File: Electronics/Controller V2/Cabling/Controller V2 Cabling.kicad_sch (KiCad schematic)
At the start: 13 parts, among them J1 776164-1, J10 Spare Valve, J11 Battery, J12 776286-1, J2 GPIO, J3 Tractor CAN, J4 Scraper CAN, J5 Spare CAN, J6 Front Height, J7 Rear Height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

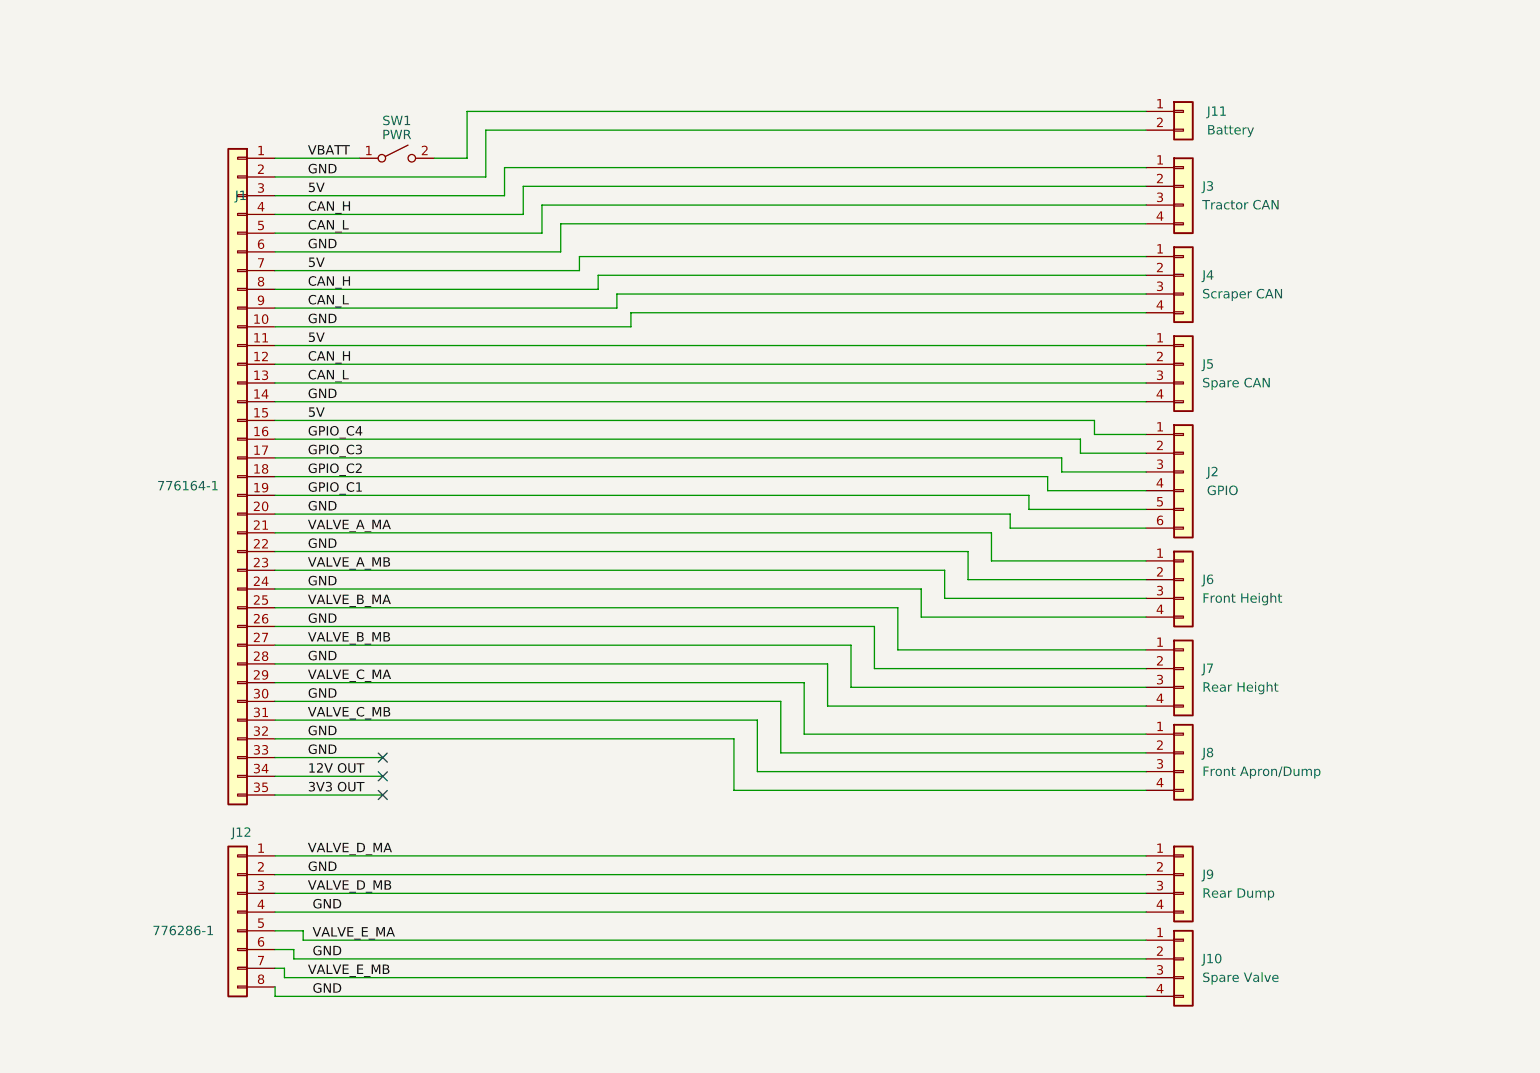
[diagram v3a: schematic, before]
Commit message: Working on autosteer support for V2 controller.
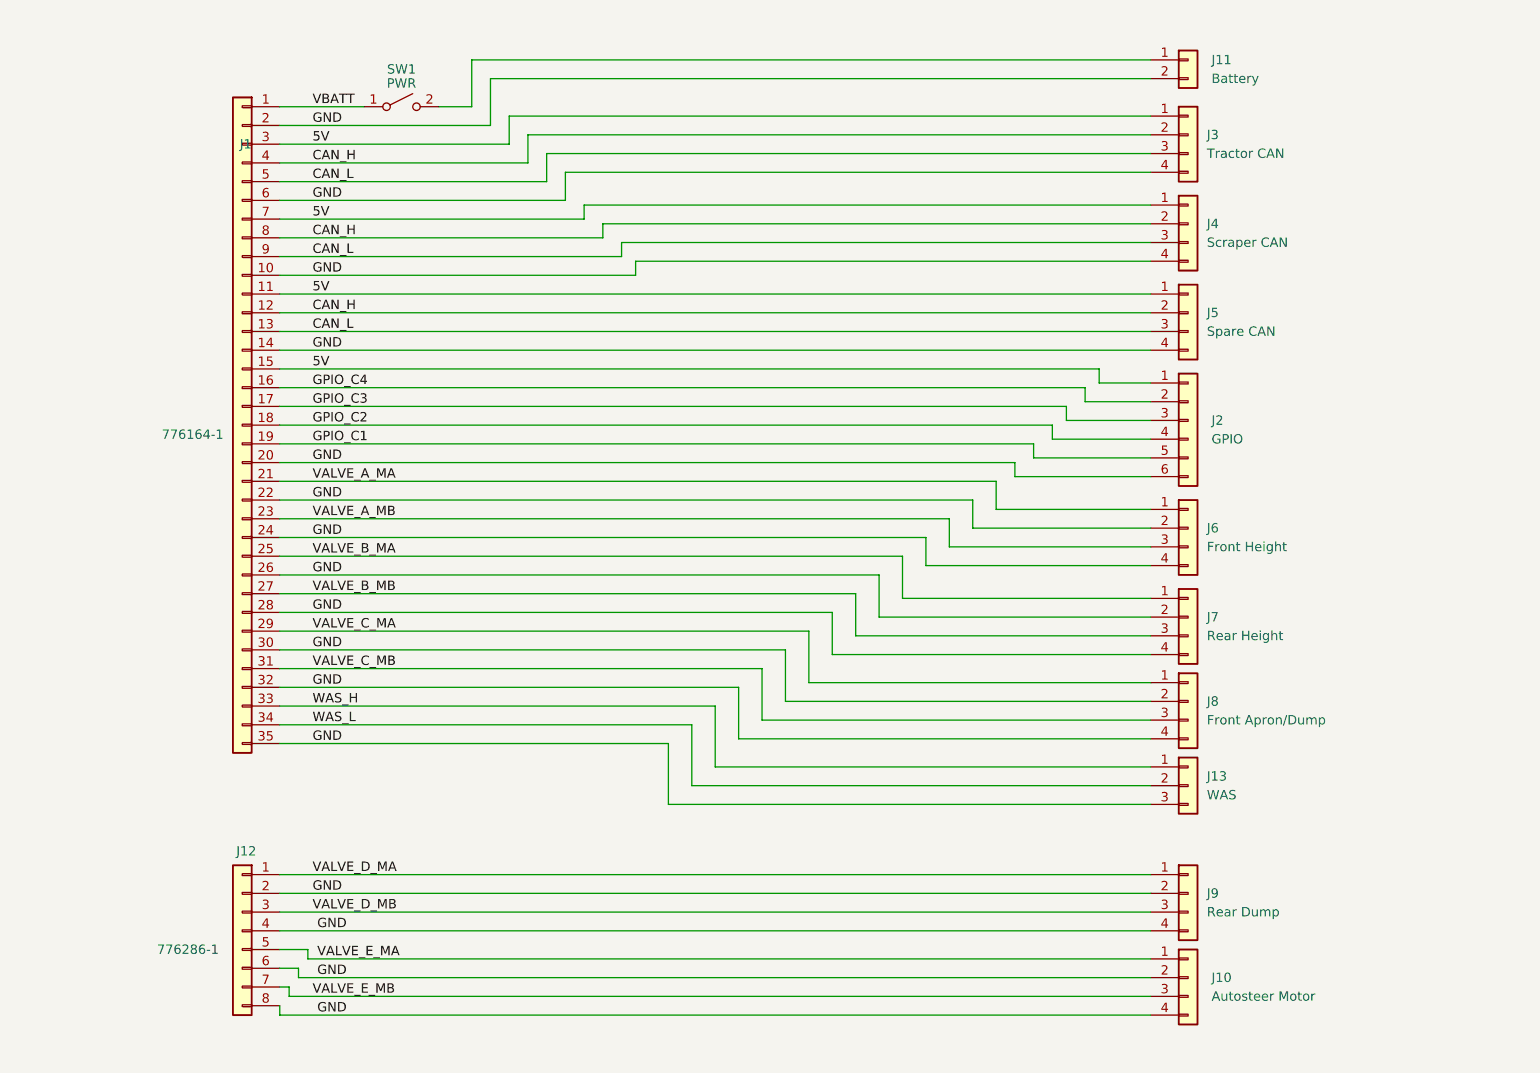
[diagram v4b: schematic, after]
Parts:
- added J13: WAS, symbol Connector_Generic:Conn_01x03
- J10: value Spare Valve -> Autosteer Motor
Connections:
- net 3V3 OUT is gone; now on net GND: J1.35 (Pin_35)
- net GND: now also J13.3 (Pin_3); no longer J1.33 (Pin_33)
- net 12V OUT renamed WAS_L
- net WAS_L: now also J13.2 (Pin_2)
- new net WAS_H: J1.33 (Pin_33), J13.1 (Pin_1)
- no-connect marks 3 -> 0
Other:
- moved on the sheet: J1, J10, J11, J12, J2, J3, J4, J5, J6, J7, J8, J9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

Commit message: Added WAS circuit.
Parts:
- J13: symbol Connector_Generic:Conn_01x03 -> Connector_Generic:Conn_01x04
- J2: symbol Connector_Generic:Conn_01x06 -> Connector_Generic:Conn_01x05
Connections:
- net 5V: now also J1.16 (Pin_16), J13.4 (Pin_4)
- net GND: now also J2.5 (Pin_5); no longer J2.6 (Pin_6)
- net GPIO_C1: now also J2.4 (Pin_4); no longer J2.5 (Pin_5)
- net GPIO_C2: now also J2.3 (Pin_3); no longer J2.4 (Pin_4)
- net GPIO_C3: now also J2.2 (Pin_2); no longer J2.3 (Pin_3)
- removed net GPIO_C4: J1.16 (Pin_16), J2.2 (Pin_2)
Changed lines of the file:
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@@
+    (stroke (width 0) (type default))
+  )
+  (wire (pts (xy 202.565 130.81) (xy 103.505 130.81))
     (stroke (width 0) (type default))
   )
@@
     (stroke (width 0) (type default))
   )
+  (wire (pts (xy 103.505 130.81) (xy 103.505 69.215))
+    (stroke (width 0) (type default))
+  )
   (wire (pts (xy 202.565 34.925) (xy 115.57 34.925))
     (stroke (width 0) (type default))
@@
     (stroke (width 0) (type default))
   )
-  (wire (pts (xy 202.565 71.12) (xy 195.58 71.12))
-    (stroke (width 0) (type default))
-  )
   (wire (pts (xy 84.455 74.295) (xy 191.135 74.295))
     (stroke (width 0) (type default))
@@
     (stroke (width 0) (type default))
   )
-  (wire (pts (xy 84.455 69.215) (xy 195.58 69.215))
-    (stroke (width 0) (type default))
-  )
   (wire (pts (xy 84.455 46.355) (xy 123.19 46.355))
     (stroke (width 0) (type default))
@@
     (stroke (width 0) (type default))
   )
+  (wire (pts (xy 84.455 69.215) (xy 103.505 69.215))
+    (stroke (width 0) (type default))
+  )
   (wire (pts (xy 202.565 52.07) (xy 130.81 52.07))
     (stroke (width 0) (type default))
@@
     (stroke (width 0) (type default))
   )
-  (wire (pts (xy 195.58 71.12) (xy 195.58 69.215))
-    (stroke (width 0) (type default))
-  )
   (wire (pts (xy 202.565 95.885) (xy 172.085 95.885))
     (stroke (width 0) (type default))
@@
     (effects (font (size 1.27 1.27)) (justify left bottom))
   )
-  (label "GPIO_C4" (at 88.9 71.755 0) (fields_autoplaced)
+  (label "5V" (at 88.9 71.755 0) (fields_autoplaced)
     (effects (font (size 1.27 1.27)) (justify left bottom))
   )
@@
     )
   )
-  (symbol (lib_id "Connector_Generic:Conn_01x06") (at 207.645 76.2 0) (unit 1)
-    (in_bom yes) (on_board yes) (dnp no) (fields_autoplaced)
-    (property "Reference" "J2" (at 210.82 76.2 0)
-      (effects (font (size 1.27 1.27)) (justify left))
-    )
-    (property "Value" "GPIO" (at 210.82 78.74 0)
-      (effects (font (size 1.27 1.27)) (justify left))
-    )
-    (property "Footprint" "" (at 207.645 76.2 0)
-      (effects (font (size 1.27 1.27)) hide)
-    )
-    (property "Datasheet" "~" (at 207.645 76.2 0)
+  (symbol (lib_id "Connector_Generic:Conn_01x05") (at 207.645 78.74 0) (unit 1)
+    (in_bom yes) (on_board yes) (dnp no) (fields_autoplaced)
+    (property "Reference" "J2" (at 210.82 77.47 0)
+      (effects (font (size 1.27 1.27)) (justify left))
+    )
+    (property "Value" "GPIO" (at 210.82 80.01 0)
+      (effects (font (size 1.27 1.27)) (justify left))
+    )
+    (property "Footprint" "" (at 207.645 78.74 0)
+      (effects (font (size 1.27 1.27)) hide)
+    )
+    (property "Datasheet" "~" (at 207.645 78.74 0)
       (effects (font (size 1.27 1.27)) hide)
     )
     (pin "5")
     (pin "1")
-    (pin "6")
     (pin "2")
     (pin "4")
@@
     )
   )
-  (symbol (lib_id "Connector_Generic:Conn_01x03") (at 207.645 125.73 0) (unit 1)
-    (in_bom yes) (on_board yes) (dnp no) (fields_autoplaced)
-    (property "Reference" "J13" (at 210.185 124.46 0)
-      (effects (font (size 1.27 1.27)) (justify left))
-    )
-    (property "Value" "WAS" (at 210.185 127 0)
+  (symbol (lib_id "Connector_Generic:Conn_01x04") (at 207.645 125.73 0) (unit 1)
+    (in_bom yes) (on_board yes) (dnp no) (fields_autoplaced)
+    (property "Reference" "J13" (at 210.82 125.73 0)
+      (effects (font (size 1.27 1.27)) (justify left))
+    )
+    (property "Value" "WAS" (at 210.82 128.27 0)
       (effects (font (size 1.27 1.27)) (justify left))
     )
@@
     (pin "1")
     (pin "2")
-    (instances
-      (project "Controller V2 Cabling"
+    (pin "4")
+    (instances
+      (project "Controller V2 Cabling"

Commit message: Added connector to valve daugherboard for optional 12V to 24V converter.
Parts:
- added F1, F2: 3A, symbol Device:Fuse
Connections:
- net VALVE_E_MA: now also F1.1; no longer J10.1 (Pin_1)
- net VALVE_E_MB: now also F2.1; no longer J10.3 (Pin_3)
- new net: F1.2, J10.1 (Pin_1)
- new net: F2.2, J10.3 (Pin_3)
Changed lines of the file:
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@@
+    (stroke (width 0) (type default))
+  )
+  (wire (pts (xy 88.265 149.225) (xy 106.045 149.225))
     (stroke (width 0) (type default))
   )
@@
     (stroke (width 0) (type default))
   )
+  (wire (pts (xy 113.665 149.225) (xy 202.565 149.225))
+    (stroke (width 0) (type default))
+  )
   (wire (pts (xy 202.565 81.28) (xy 186.69 81.28))
     (stroke (width 0) (type default))
@@
     (stroke (width 0) (type default))
   )
+  (wire (pts (xy 113.665 154.305) (xy 202.565 154.305))
+    (stroke (width 0) (type default))
+  )
   (wire (pts (xy 140.335 125.73) (xy 202.565 125.73))
     (stroke (width 0) (type default))
@@
     (stroke (width 0) (type default))
   )
-  (wire (pts (xy 85.725 154.305) (xy 202.565 154.305))
-    (stroke (width 0) (type default))
-  )
   (wire (pts (xy 202.565 37.465) (xy 118.11 37.465))
     (stroke (width 0) (type default))
   )
+  (wire (pts (xy 85.725 154.305) (xy 106.045 154.305))
+    (stroke (width 0) (type default))
+  )
   (wire (pts (xy 186.69 81.28) (xy 186.69 79.375))
     (stroke (width 0) (type default))
@@
   )
   (wire (pts (xy 202.565 40.005) (xy 120.65 40.005))
-    (stroke (width 0) (type default))
-  )
-  (wire (pts (xy 88.265 149.225) (xy 202.565 149.225))
     (stroke (width 0) (type default))
   )
@@
         (path "/0b1bc3d2-0feb-4765-8c0c-3c48ba6f9919"
           (reference "J8") (unit 1)
+        )
+      )
+    )
+  )
+  (symbol (lib_id "Device:Fuse") (at 109.855 149.225 90) (unit 1)
+    (in_bom yes) (on_board yes) (dnp no)
+    (property "Reference" "F1" (at 105.41 150.495 90)
+      (effects (font (size 1.27 1.27)))
+    )
+    (property "Value" "3A" (at 105.41 147.955 90)
+      (effects (font (size 1.27 1.27)))
+    )
+    (property "Footprint" "" (at 109.855 151.003 90)
+      (effects (font (size 1.27 1.27)) hide)
+    )
+    (property "Datasheet" "~" (at 109.855 149.225 0)
+      (effects (font (size 1.27 1.27)) hide)
+    )
+    (pin "1")
+    (pin "2")
+    (instances
+      (project "Controller V2 Cabling"
+        (path "/0b1bc3d2-0feb-4765-8c0c-3c48ba6f9919"
+          (reference "F1") (unit 1)
         )
       )
@@
         )
       )
+    )
+  )
+  (symbol (lib_id "Device:Fuse") (at 109.855 154.305 90) (unit 1)
+    (in_bom yes) (on_board yes) (dnp no)
+    (property "Reference" "F2" (at 105.41 155.575 90)
+      (effects (font (size 1.27 1.27)))
+    )
+    (property "Value" "3A" (at 105.41 153.035 90)
+      (effects (font (size 1.27 1.27)))
+    )
+    (property "Footprint" "" (at 109.855 156.083 90)
+      (effects (font (size 1.27 1.27)) hide)
+    )
+    (property "Datasheet" "~" (at 109.855 154.305 0)
+      (effects (font (size 1.27 1.27)) hide)
+    )
+    (pin "1")
+    (pin "2")
+    (instances
+      (project "Controller V2 Cabling"
+        (path "/0b1bc3d2-0feb-4765-8c0c-3c48ba6f9919"
+          (reference "F2") (unit 1)
+        )
+      )

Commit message: Updated housing cutouts for M12 connectors. Added M12 female cable ends to check for clearances.
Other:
- note added: "FEMALE XLR"
- note added: "MALE XLR"
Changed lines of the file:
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@@
     (stroke (width 0) (type default))
+  )
+  (text "FEMALE XLR" (at 230.505 40.005 0)
+    (effects (font (size 1.27 1.27)) (justify left bottom))
+  )
+  (text "FEMALE XLR" (at 230.505 51.435 0)
+    (effects (font (size 1.27 1.27)) (justify left bottom))
+  )
+  (text "MALE XLR" (at 230.505 153.67 0)
+    (effects (font (size 1.27 1.27)) (justify left bottom))
+  )
+  (text "MALE XLR" (at 230.505 92.71 0)
+    (effects (font (size 1.27 1.27)) (justify left bottom))
+  )
+  (text "MALE XLR" (at 230.505 104.775 0)
+    (effects (font (size 1.27 1.27)) (justify left bottom))
+  )
+  (text "FEMALE XLR" (at 230.505 78.74 0)
+    (effects (font (size 1.27 1.27)) (justify left bottom))
+  )
+  (text "MALE XLR" (at 230.505 142.24 0)
+    (effects (font (size 1.27 1.27)) (justify left bottom))
+  )
+  (text "MALE XLR" (at 230.505 127.635 0)
+    (effects (font (size 1.27 1.27)) (justify left bottom))
+  )
+  (text "MALE XLR" (at 230.505 116.205 0)
+    (effects (font (size 1.27 1.27)) (justify left bottom))
+  )
+  (text "FEMALE XLR" (at 230.505 62.865 0)
+    (effects (font (size 1.27 1.27)) (justify left bottom))
   )
   (label "GND" (at 88.9 102.235 0) (fields_autoplaced)
